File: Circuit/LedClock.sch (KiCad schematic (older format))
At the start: 21 parts, among them U1 MSP430G2553IPW20

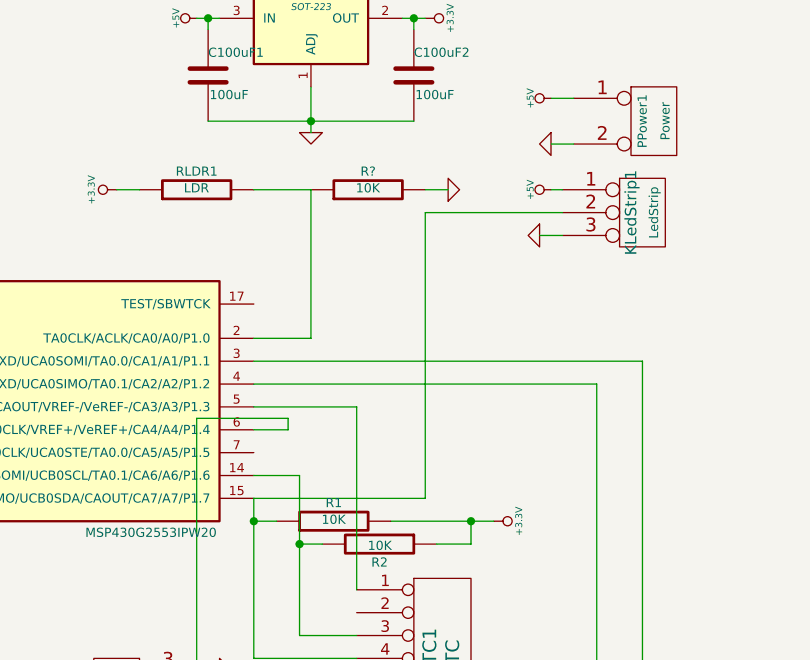
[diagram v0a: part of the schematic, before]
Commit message: Added current limiting resistor on the ledstrip data line Adviced by adafruit
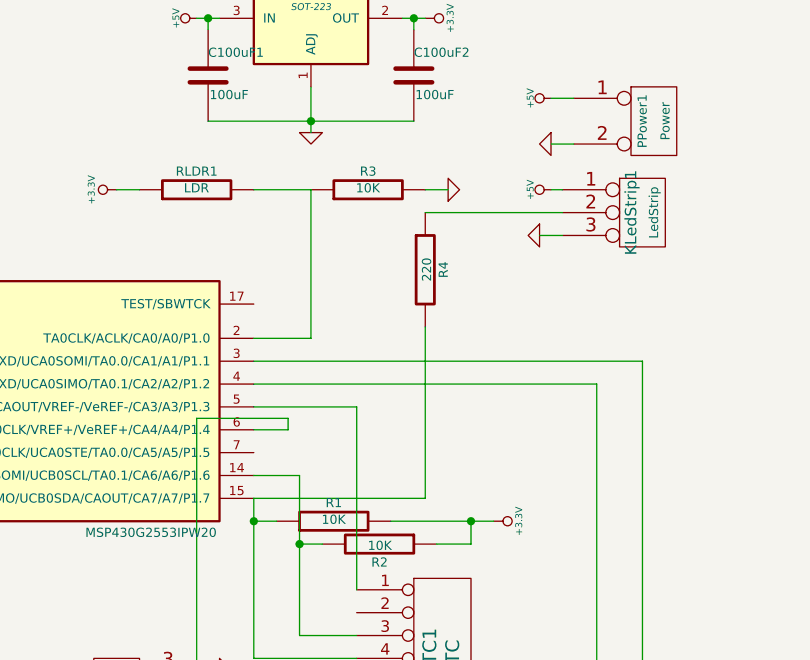
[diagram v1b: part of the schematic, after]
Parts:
- added R4: 220, ~, symbol R
- gave numbers to parts that had none: 1
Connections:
- net at PRTC1.4 (P4), R1.1, U1.15 (TDO/TDI/UCB0SIMO/UCB0SDA/CAOUT/CA7/A7/P1.7): now also R4.2; no longer KLedStrip1.2 (PM)
- new net: KLedStrip1.2 (PM), R4.1

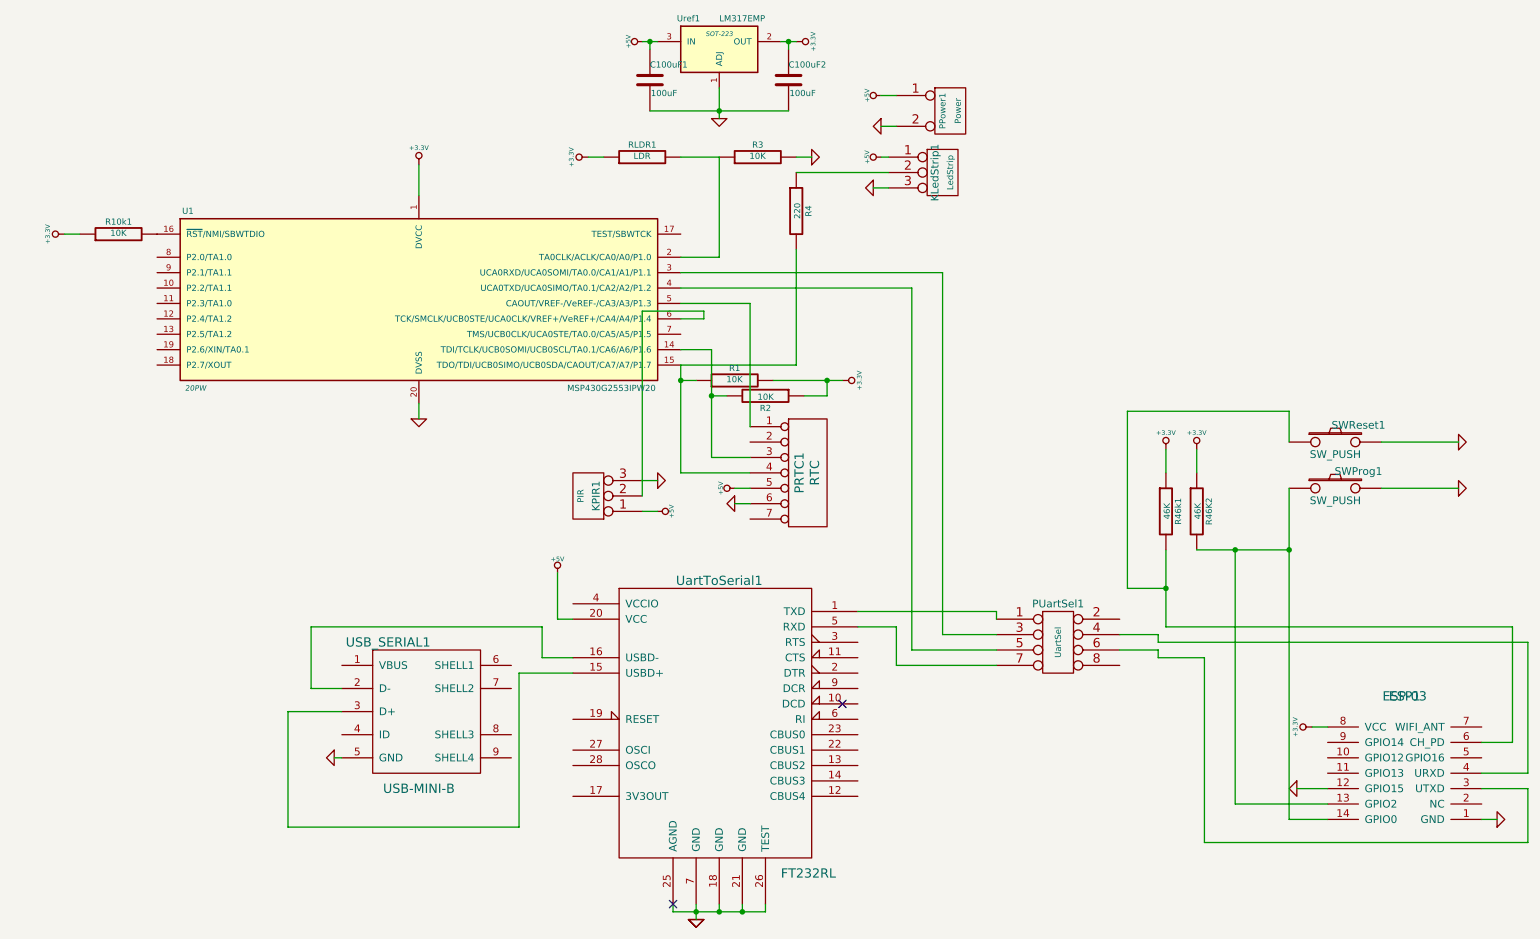
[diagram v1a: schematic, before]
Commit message: Updated layout to fit the new ring and stay within 10*5cm
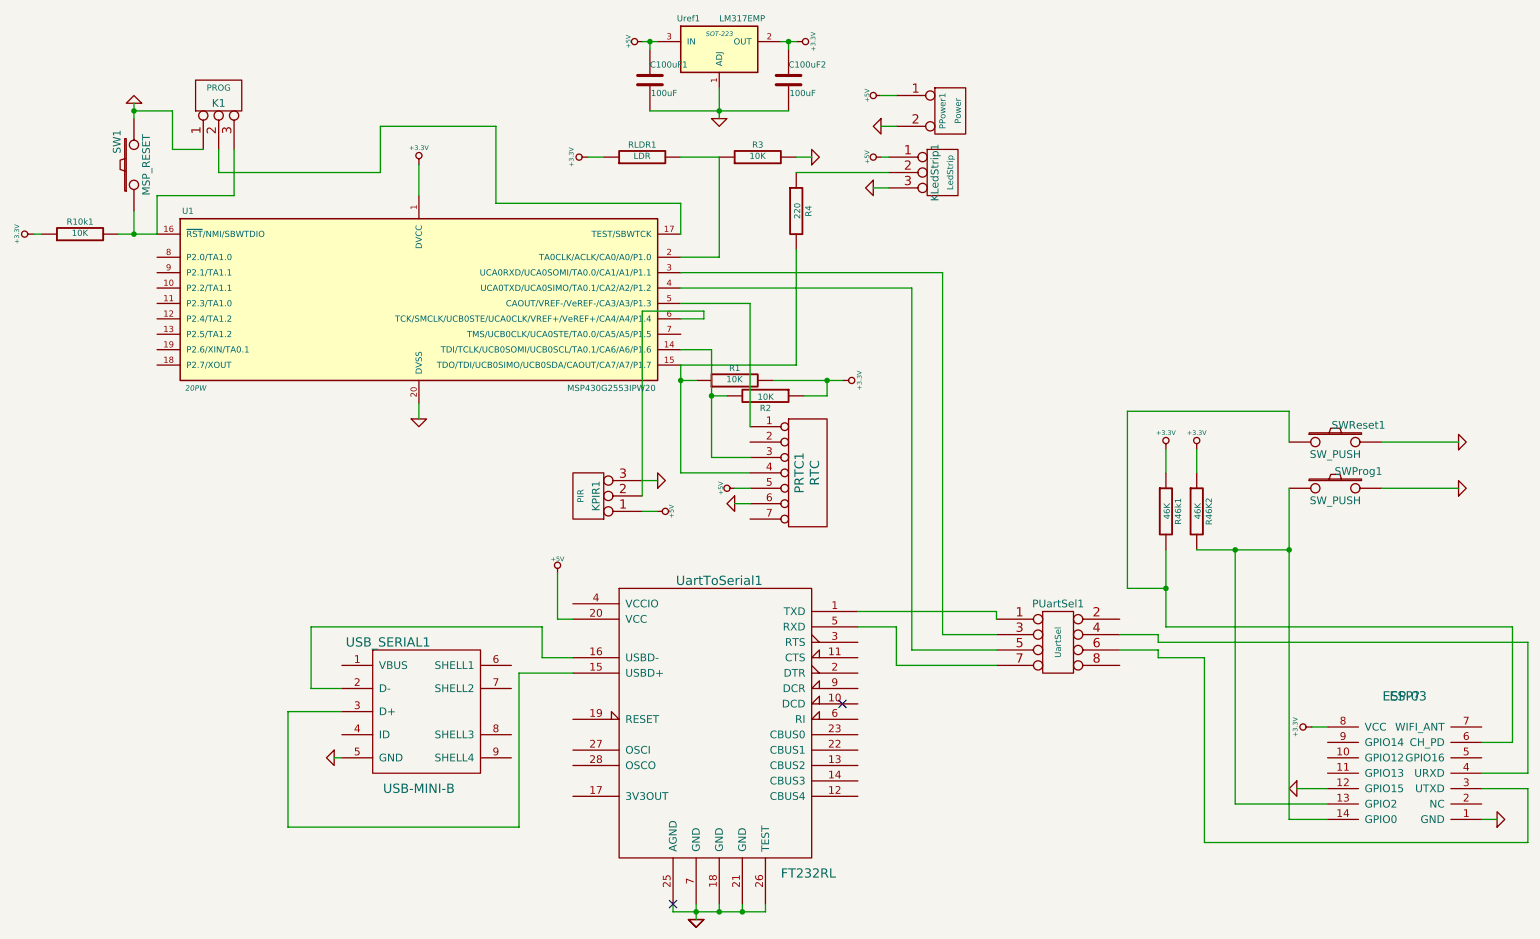
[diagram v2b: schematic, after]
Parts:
- removed ESP1: ESP-03, symbol ESP-03
- added ESP?: ESP-03, symbol ESP-03
- added K1: PROG, symbol CONN_3
- added SW1: MSP_RESET, ~, symbol SW_PUSH
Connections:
- net +3.3V: now also ESP?.8 (VCC)
- net GND: now also ESP?.1 (GND), ESP?.12 (GPIO15), K1.1 (P1), SW1.2
- net at R10k1.2, U1.16 (~RST~/NMI/SBWTDIO): now also K1.3 (P3), SW1.1
- net at U1.17 (TEST/SBWTCK): now also K1.2 (PM)
- net at PUartSel1.4: now also ESP?.4 (URXD)
- net at PUartSel1.6: now also ESP?.3 (UTXD)
- net at R46k1.2, SWReset1.1: now also ESP?.6 (CH_PD)
- net at R46K2.2, SWProg1.1: now also ESP?.13 (GPIO2), ESP?.14 (GPIO0)
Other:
- moved on the sheet: R10k1
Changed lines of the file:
@@
 Sheet 1 1
 Title ""
-Date "5 sep 2015"
+Date "26 sep 2015"
 Rev ""
 Comp ""
@@
 $EndComp
 $Comp
-L GND #PWR2
+L GND #PWR3
 U 1 1 55E4A1E2
 P 2950 5550
-F 0 "#PWR2" H 2950 5550 30  0001 C CNN
+F 0 "#PWR3" H 2950 5550 30  0001 C CNN
 F 1 "GND" H 2950 5480 30  0001 C CNN
 F 2 "" H 2950 5550 60  0000 C CNN
@@
 $EndComp
 $Comp
-L GND #PWR10
+L GND #PWR11
 U 1 1 55E4A206
-P 5300 6600
-F 0 "#PWR10" H 5300 6600 30  0001 C CNN
-F 1 "GND" H 5300 6530 30  0001 C CNN
-F 2 "" H 5300 6600 60  0000 C CNN
-F 3 "" H 5300 6600 60  0000 C CNN
-	1    5300 6600
-	1    0    0    -1
-$EndComp
-$Comp
-L GND #PWR11
-U 1 1 55E4A213
 P 5300 6600
 F 0 "#PWR11" H 5300 6600 30  0001 C CNN
@@
 $EndComp
 $Comp
-L GND #PWR4
+L GND #PWR12
+U 1 1 55E4A213
+P 5300 6600
+F 0 "#PWR12" H 5300 6600 30  0001 C CNN
+F 1 "GND" H 5300 6530 30  0001 C CNN
+F 2 "" H 5300 6600 60  0000 C CNN
+F 3 "" H 5300 6600 60  0000 C CNN
+	1    5300 6600
+	1    0    0    -1
+$EndComp
+$Comp
+L GND #PWR5
 U 1 1 55E4A237
 P 3500 3350
-F 0 "#PWR4" H 3500 3350 30  0001 C CNN
+F 0 "#PWR5" H 3500 3350 30  0001 C CNN
 F 1 "GND" H 3500 3280 30  0001 C CNN
 F 2 "" H 3500 3350 60  0000 C CNN
@@
 $EndComp
 $Comp
-L GND #PWR12
+L GND #PWR13
 U 1 1 55E4A246
 P 5450 1400
-F 0 "#PWR12" H 5450 1400 30  0001 C CNN
+F 0 "#PWR13" H 5450 1400 30  0001 C CNN
 F 1 "GND" H 5450 1330 30  0001 C CNN
 F 2 "" H 5450 1400 60  0000 C CNN
@@
 $EndComp
 $Comp
-L +5V #PWR7
+L +5V #PWR8
 U 1 1 55E4A25B
 P 4950 900
-F 0 "#PWR7" H 4950 990 20  0001 C CNN
+F 0 "#PWR8" H 4950 990 20  0001 C CNN
 F 1 "+5V" H 4950 990 30  0000 C CNN
 F 2 "" H 4950 900 60  0000 C CNN
@@
 $EndComp
 $Comp
-L +3.3V #PWR15
+L +3.3V #PWR16
 U 1 1 55E4A26A
 P 5950 900
-F 0 "#PWR15" H 5950 860 30  0001 C CNN
+F 0 "#PWR16" H 5950 860 30  0001 C CNN
 F 1 "+3.3V" H 5950 1010 30  0000 C CNN
 F 2 "" H 5950 900 60  0000 C CNN
@@
 $EndComp
 $Comp
-L +3.3V #PWR3
+L +3.3V #PWR4
 U 1 1 55E4A279
 P 3500 1700
-F 0 "#PWR3" H 3500 1660 30  0001 C CNN
+F 0 "#PWR4" H 3500 1660 30  0001 C CNN
 F 1 "+3.3V" H 3500 1810 30  0000 C CNN
 F 2 "" H 3500 1700 60  0000 C CNN
@@
 $EndComp
 $Comp
-L +5V #PWR21
+L +5V #PWR22
 U 1 1 55E4A420
 P 6500 1650
-F 0 "#PWR21" H 6500 1740 20  0001 C CNN
+F 0 "#PWR22" H 6500 1740 20  0001 C CNN
 F 1 "+5V" H 6500 1740 30  0000 C CNN
 F 2 "" H 6500 1650 60  0000 C CNN
@@
 $EndComp
 $Comp
-L +5V #PWR19
+L +5V #PWR20
 U 1 1 55E4A43E
 P 6500 1250
-F 0 "#PWR19" H 6500 1340 20  0001 C CNN
+F 0 "#PWR20" H 6500 1340 20  0001 C CNN
 F 1 "+5V" H 6500 1340 30  0000 C CNN
 F 2 "" H 6500 1250 60  0000 C CNN
@@
 $EndComp
 $Comp
-L GND #PWR20
+L GND #PWR21
 U 1 1 55E4A44D
 P 6500 1450
-F 0 "#PWR20" H 6500 1450 30  0001 C CNN
+F 0 "#PWR21" H 6500 1450 30  0001 C CNN
 F 1 "GND" H 6500 1380 30  0001 C CNN
 F 2 "" H 6500 1450 60  0000 C CNN
@@
 $EndComp
 $Comp
-L GND #PWR18
+L GND #PWR19
 U 1 1 55E4A484
 P 6450 1850
-F 0 "#PWR18" H 6450 1850 30  0001 C CNN
+F 0 "#PWR19" H 6450 1850 30  0001 C CNN
 F 1 "GND" H 6450 1780 30  0001 C CNN
 F 2 "" H 6450 1850 60  0000 C CNN
@@
 $EndComp
 $Comp
-L +5V #PWR13
+L +5V #PWR14
 U 1 1 55E4A6A8
 P 5550 3800
-F 0 "#PWR13" H 5550 3890 20  0001 C CNN
+F 0 "#PWR14" H 5550 3890 20  0001 C CNN
 F 1 "+5V" H 5550 3890 30  0000 C CNN
 F 2 "" H 5550 3800 60  0000 C CNN
@@
 $EndComp
 $Comp
-L GND #PWR14
+L GND #PWR15
 U 1 1 55E4A6BC
 P 5550 3900
-F 0 "#PWR14" H 5550 3900 30  0001 C CNN
+F 0 "#PWR15" H 5550 3900 30  0001 C CNN
 F 1 "GND" H 5550 3830 30  0001 C CNN
 F 2 "" H 5550 3900 60  0000 C CNN
@@
 $EndComp
 $Comp
-L +5V #PWR9
+L +5V #PWR10
 U 1 1 55E4A906
 P 5050 3950
-F 0 "#PWR9" H 5050 4040 20  0001 C CNN
+F 0 "#PWR10" H 5050 4040 20  0001 C CNN
 F 1 "+5V" H 5050 4040 30  0000 C CNN
 F 2 "" H 5050 3950 60  0000 C CNN
@@
 $EndComp
 $Comp
-L GND #PWR8
+L GND #PWR9
 U 1 1 55E4A924
 P 5050 3750
-F 0 "#PWR8" H 5050 3750 30  0001 C CNN
+F 0 "#PWR9" H 5050 3750 30  0001 C CNN
 F 1 "GND" H 5050 3680 30  0001 C CNN
 F 2 "" H 5050 3750 60  0000 C CNN
@@
 $EndComp
 $Comp
-L +3.3V #PWR6
+L +3.3V #PWR7
 U 1 1 55E4AA03
 P 4600 1650
-F 0 "#PWR6" H 4600 1610 30  0001 C CNN
+F 0 "#PWR7" H 4600 1610 30  0001 C CNN
 F 1 "+3.3V" H 4600 1760 30  0000 C CNN
 F 2 "" H 4600 1650 60  0000 C CNN
@@
 L R R10k1
 U 1 1 55E4AC72
-P 1550 2150
-F 0 "R10k1" V 1630 2150 40  0000 C CNN
-F 1 "10K" V 1557 2151 40  0000 C CNN
-F 2 "~" V 1480 2150 30  0000 C CNN
-F 3 "~" H 1550 2150 30  0000 C CNN
-	1    1550 2150
+P 1300 2150
+F 0 "R10k1" V 1380 2150 40  0000 C CNN
+F 1 "10K" V 1307 2151 40  0000 C CNN
+F 2 "~" V 1230 2150 30  0000 C CNN
+F 3 "~" H 1300 2150 30  0000 C CNN
+	1    1300 2150
 	0    -1   -1   0
 $EndComp
@@
 L +3.3V #PWR1
 U 1 1 55E4AC9A
-P 1200 2150
-F 0 "#PWR1" H 1200 2110 30  0001 C CNN
-F 1 "+3.3V" H 1200 2260 30  0000 C CNN
-F 2 "" H 1200 2150 60  0000 C CNN
-F 3 "" H 1200 2150 60  0000 C CNN
-	1    1200 2150
+P 1000 2150
+F 0 "#PWR1" H 1000 2110 30  0001 C CNN
+F 1 "+3.3V" H 1000 2260 30  0000 C CNN
+F 2 "" H 1000 2150 60  0000 C CNN
+F 3 "" H 1000 2150 60  0000 C CNN
+	1    1000 2150
 	0    -1   -1   0
 $EndComp
@@
 NoConn ~ 5150 6500
 $Comp
-L +5V #PWR5
+L +5V #PWR6
 U 1 1 55E4B03E
 P 4400 4350
-F 0 "#PWR5" H 4400 4440 20  0001 C CNN
+F 0 "#PWR6" H 4400 4440 20  0001 C CNN
 F 1 "+5V" H 4400 4440 30  0000 C CNN
 F 2 "" H 4400 4350 60  0000 C CNN
@@
 $EndComp
 $Comp
-L GND #PWR24
+L GND #PWR25
 U 1 1 55E4B9D8
 P 9200 5750
-F 0 "#PWR24" H 9200 5750 30  0001 C CNN
+F 0 "#PWR25" H 9200 5750 30  0001 C CNN
 F 1 "GND" H 9200 5680 30  0001 C CNN
 F 2 "" H 9200 5750 60  0000 C CNN
@@
 $EndComp
 $Comp
-L GND #PWR28
+L GND #PWR29
 U 1 1 55E4B9E7
 P 10500 5950
-F 0 "#PWR28" H 10500 5950 30  0001 C CNN
+F 0 "#PWR29" H 10500 5950 30  0001 C CNN
 F 1 "GND" H 10500 5880 30  0001 C CNN
 F 2 "" H 10500 5950 60  0000 C CNN
@@
 $EndComp
 $Comp
-L +3.3V #PWR25
+L +3.3V #PWR26
 U 1 1 55E4BA14
 P 9300 5350
-F 0 "#PWR25" H 9300 5310 30  0001 C CNN
+F 0 "#PWR26" H 9300 5310 30  0001 C CNN
 F 1 "+3.3V" H 9300 5460 30  0000 C CNN
 F 2 "" H 9300 5350 60  0000 C CNN
@@
 $EndComp
 $Comp
-L GND #PWR26
+L GND #PWR27
 U 1 1 55E4BFAA
 P 10250 3500
-F 0 "#PWR26" H 10250 3500 30  0001 C CNN
+F 0 "#PWR27" H 10250 3500 30  0001 C CNN
 F 1 "GND" H 10250 3430 30  0001 C CNN
 F 2 "" H 10250 3500 60  0000 C CNN
@@
 $EndComp
 $Comp
-L +3.3V #PWR23
+L +3.3V #PWR24
 U 1 1 55E4C0BC
 P 8550 3550
-F 0 "#PWR23" H 8550 3510 30  0001 C CNN
+F 0 "#PWR24" H 8550 3510 30  0001 C CNN
 F 1 "+3.3V" H 8550 3660 30  0000 C CNN
 F 2 "" H 8550 3550 60  0000 C CNN
@@
 $EndComp
 $Comp
-L +3.3V #PWR22
+L +3.3V #PWR23
 U 1 1 55E4C1D5
 P 8350 3550
-F 0 "#PWR22" H 8350 3510 30  0001 C CNN
+F 0 "#PWR23" H 8350 3510 30  0001 C CNN
 F 1 "+3.3V" H 8350 3660 30  0000 C CNN
 F 2 "" H 8350 3550 60  0000 C CNN
@@
 $EndComp
 $Comp
-L GND #PWR27
+L GND #PWR28
 U 1 1 55E4C1DC
 P 10250 3800
-F 0 "#PWR27" H 10250 3800 30  0001 C CNN
+F 0 "#PWR28" H 10250 3800 30  0001 C CNN
 F 1 "GND" H 10250 3730 30  0001 C CNN
 F 2 "" H 10250 3800 60  0000 C CNN
@@
 $EndComp
 $Comp
-L +3.3V #PWR17
+L +3.3V #PWR18
 U 1 1 55E89C3F
 P 6250 3100
-F 0 "#PWR17" H 6250 3060 30  0001 C CNN
+F 0 "#PWR18" H 6250 3060 30  0001 C CNN
 F 1 "+3.3V" H 6250 3210 30  0000 C CNN
 F 2 "" H 6250 3100 60  0000 C CNN
@@
 	1    6250 3100
 	0    1    1    0
-$EndComp
-$Comp
-L ESP-03 ESP1
-U 1 1 55E9DB43
-P 9900 5150
-F 0 "ESP1" H 9900 5150 60  0000 C CNN
-F 1 "ESP-03" H 9900 5150 60  0000 C CNN
-F 2 "" H 9900 5150 60  0000 C CNN
-F 3 "" H 9900 5150 60  0000 C CNN
-	1    9900 5150
-	1    0    0    -1
 $EndComp
 $Comp
@@
 $EndComp
 $Comp
-L GND #PWR16
+L GND #PWR17
 U 1 1 55E9E6F2
 P 6050 1650
-F 0 "#PWR16" H 6050 1650 30  0001 C CNN
+F 0 "#PWR17" H 6050 1650 30  0001 C CNN
 F 1 "GND" H 6050 1580 30  0001 C CNN
 F 2 "" H 6050 1650 60  0000 C CNN
@@
 Wire Wire Line
 	4600 1650 4700 1650
-Wire Wire Line
-	1300 2150 1200 2150
 Wire Wire Line
 	5450 6500 5450 6550
@@
 Wire Wire Line
 	5950 3000 5950 2250
+Wire Wire Line
+	1800 2150 1550 2150
+Wire Wire Line
+	1050 2150 1000 2150
+$Comp
+L SW_PUSH SW1
+U 1 1 56006916
+P 1650 1700
+F 0 "SW1" H 1800 1810 50  0000 C CNN
+F 1 "MSP_RESET" H 1650 1620 50  0000 C CNN
+F 2 "~" H 1650 1700 60  0000 C CNN
+F 3 "~" H 1650 1700 60  0000 C CNN
+	1    1650 1700
+	0    -1   -1   0
+$EndComp
+Wire Wire Line
+	1650 2000 1650 2150
+Connection ~ 1650 2150
+$Comp
+L GND #PWR2
+U 1 1 5600699A
+P 1650 1300
+F 0 "#PWR2" H 1650 1300 30  0001 C CNN
+F 1 "GND" H 1650 1230 30  0001 C CNN
+F 2 "" H 1650 1300 60  0000 C CNN
+F 3 "" H 1650 1300 60  0000 C CNN
+	1    1650 1300
+	-1   0    0    1
+$EndComp
+Wire Wire Line
+	1650 1400 1650 1300
+$Comp
+L CONN_3 K1
+U 1 1 56006A20
+P 2200 1250
+F 0 "K1" V 2150 1250 50  0000 C CNN
+F 1 "PROG" V 2250 1250 40  0000 C CNN
+F 2 "" H 2200 1250 60  0000 C CNN
+F 3 "" H 2200 1250 60  0000 C CNN
+	1    2200 1250
+	0    -1   -1   0
+$EndComp
+Wire Wire Line
+	1650 1350 1900 1350
+Wire Wire Line
+	1900 1350 1900 1600
+Wire Wire Line
+	1900 1600 2100 1600
+Connection ~ 1650 1350
+Wire Wire Line
+	2200 1600 2200 1750
+Wire Wire Line
+	2200 1750 3250 1750
+Wire Wire Line
+	3250 1750 3250 1450
+Wire Wire Line
+	3250 1450 4000 1450
+Wire Wire Line
+	4000 1450 4000 1950
+Wire Wire Line
+	4000 1950 5200 1950
+Wire Wire Line
+	5200 1950 5200 2150
+Wire Wire Line
+	2300 1600 2300 1900
+Wire Wire Line
+	2300 1900 1800 1900
+Wire Wire Line
+	1800 1900 1800 2150
+$Comp
+L ESP-03 ESP?
+U 1 1 56066F62
+P 9900 5150
+F 0 "ESP?" H 9900 5150 60  0000 C CNN
+F 1 "ESP-03" H 9900 5150 60  0000 C CNN
+F 2 "" H 9900 5150 60  0000 C CNN
+F 3 "" H 9900 5150 60  0000 C CNN
+	1    9900 5150
+	1    0    0    -1
+$EndComp
 $EndSCHEMATC

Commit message: Updated schematic
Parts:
- gave numbers to parts that had none: 1
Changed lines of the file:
@@
 	1800 1900 1800 2150
 $Comp
-L ESP-03 ESP?
+L ESP-03 ESP1
 U 1 1 56066F62
 P 9900 5150
-F 0 "ESP?" H 9900 5150 60  0000 C CNN
+F 0 "ESP1" H 9900 5150 60  0000 C CNN
 F 1 "ESP-03" H 9900 5150 60  0000 C CNN
 F 2 "" H 9900 5150 60  0000 C CNN

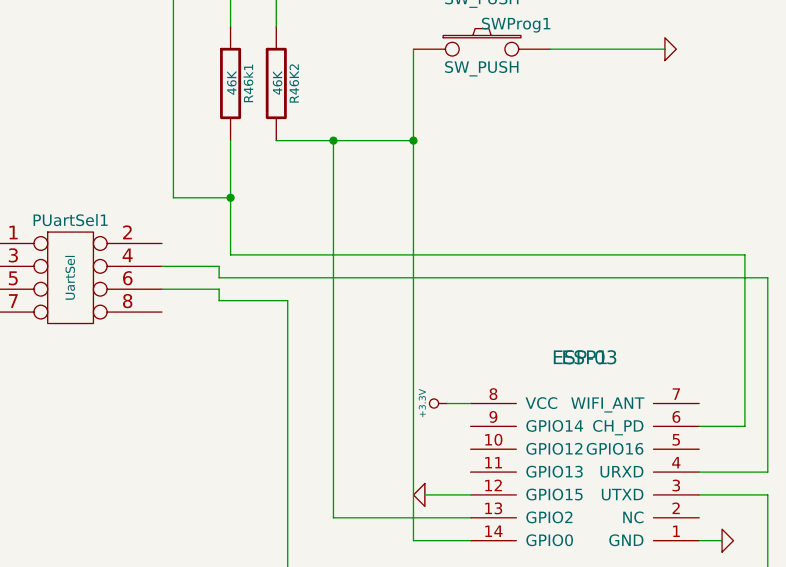
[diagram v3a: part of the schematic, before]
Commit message: Updated pcb with cutting edges, fixed minor issue and put name and version on pcb
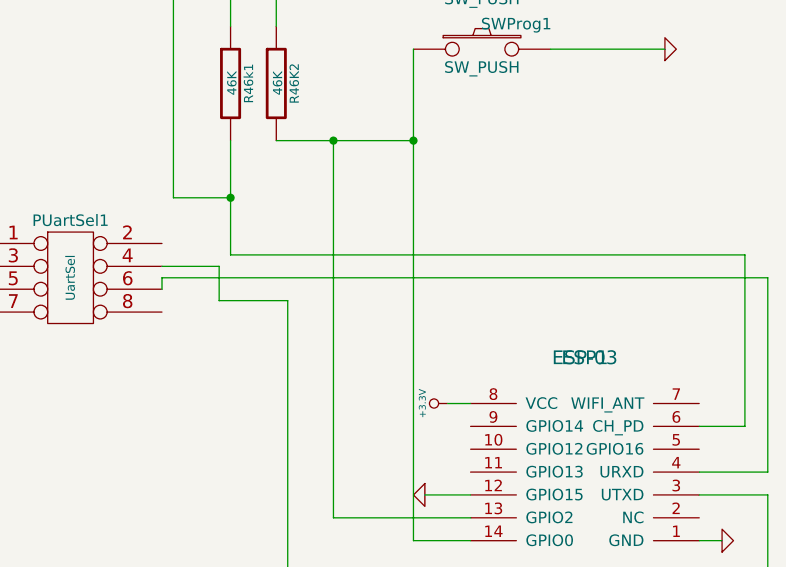
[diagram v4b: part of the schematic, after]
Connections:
- net at PUartSel1.4: now also ESP1.3 (UTXD); no longer ESP1.4 (URXD)
- net at PUartSel1.6: now also ESP1.4 (URXD); no longer ESP1.3 (UTXD)
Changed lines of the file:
@@
 Sheet 1 1
 Title ""
-Date "26 sep 2015"
+Date "10 jan 2016"
 Rev ""
 Comp ""
@@
 	7250 4600 7250 4650
 Wire Wire Line
-	8300 4800 8300 4750
-Wire Wire Line
-	8300 4750 8050 4750
-Wire Wire Line
-	8300 4900 8300 4850
-Wire Wire Line
-	8300 4850 8050 4850
-Wire Wire Line
 	9750 3500 10250 3500
 Wire Wire Line
@@
 	10700 5750 10400 5750
 Wire Wire Line
-	8300 4800 10700 4800
+	8050 4800 10700 4800
 Wire Wire Line
 	8300 4900 8600 4900
@@
 	1    0    0    -1
 $EndComp
+Wire Wire Line
+	8050 4800 8050 4850
+Wire Wire Line
+	8300 4900 8300 4750
+Wire Wire Line
+	8300 4750 8050 4750
 $EndSCHEMATC
